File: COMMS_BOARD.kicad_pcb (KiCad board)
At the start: 4 copper layers, 75 x 55 mm, 107 parts, among them IC1 TCAN1044VDDFR, IC2 BMM350, J1 Conn_Coaxial_Small, J2 Conn_01x02, J3 Conn_01x04, J4 Screw_Terminal_01x02, J5 Conn_01x02, J6 Conn_Coaxial_Small, J7 Conn_01x06, J8 Conn_01x04, U1 MAX31855KASA, U2 SA818V, U3 ESP32-WROOM-32E, U4 MAX-M10S, U5 USBLC6-2SC6, U6 MS5611-01BA

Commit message: ADDE IMU
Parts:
- removed D3, D8: PESD3V3Z1BCSFYL, SamacSys_Parts:PMEG3005AESFYL
- added C28: 100nF, Capacitor_SMD:C_0603_1608Metric, F.Cu at (155.2, 78.2)
- added C29: 100nF, Capacitor_SMD:C_0603_1608Metric, F.Cu at (155.3, 80.2)
- added U7: BMI088, Package_LGA:Bosch_LGA-16_4.5x3mm_P0.5mm_LayoutBorder7x1y_ClockwisePinNumbering, F.Cu at (155.1, 83.0)
- J5: value Conn_01x02 -> S2B-PH-SM4-TB_LF__SN_; footprint Connector_JST:JST_XH_B2B-XH-A_1x02_P2.50mm_Vertical -> SamacSys_Parts:S2BPHSM4TBLFSN; moved to B.Cu
- J7: value Conn_01x06 -> Conn_01x04; footprint Connector_JST:JST_PH_B6B-PH-K_1x06_P2.00mm_Vertical -> Connector_JST:JST_PH_S4B-PH-K_1x04_P2.00mm_Horizontal
- R3: moved to F.Cu
- moved R10 8.40 mm to (146.4, 78.8), turned to -90 degrees
- moved R9 8.36 mm to (146.4, 82.0), turned to 90 degrees
- moved J5 6.97 mm to (141.7, 100.2)
- moved C25 5.27 mm to (160.3, 102.8)
- moved C26 5.27 mm to (156.7, 100.1)
- moved C27 5.27 mm to (161.7, 100.0)
- moved IC2 5.27 mm to (159.2, 99.8)
- moved C23 5.10 mm to (158.4, 93.7)
- moved C24 5.10 mm to (156.6, 93.7)
- moved U6 5.10 mm to (161.2, 93.8)
- moved C3 4.50 mm to (165.7, 74.3)
- moved R3 2.95 mm to (144.2, 78.8), turned to 90 degrees
- moved J7 2.87 mm to (142.9, 87.9)
- moved R2 2.11 mm to (167.6, 74.2), turned to 90 degrees
- moved S2 1.26 mm to (140.2, 80.3)
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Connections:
- J5 pad 1: CAN+ -> CAN-
- J5 pad 2: CAN- -> CAN+
- J7 pad 4: CUTTER_EN -> GND
- U3 pad 6: CUTTER_EN -> INT1_ACCEL
- U3 pad 7: VTX_EN -> INT1_GYRO
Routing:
- net VTX_EN: track 45.2 -> 0.00 mm, vias 2 -> 0
- net CUTTER_EN: track 44.1 -> 0.00 mm, vias 2 -> 0
- net I2C_SDL: track 89.4 -> 109.0 mm, vias 11 -> 10
- net INT1_ACCEL: track 0.00 -> 17.0 mm, vias 0 -> 1
- net I2C_SDA: track 84.0 -> 97.0 mm
- net GND: track 69.0 -> 80.2 mm, vias 416 -> 290
- net INT1_GYRO: track 0.00 -> 10.0 mm, vias 0 -> 1
- net BOOT: track 45.4 -> 53.1 mm, vias 1 -> 2
- net +3V3: track 45.7 -> 50.1 mm, vias 35 -> 37
- net CAN-: track 23.9 -> 27.8 mm, vias 0 -> 2
- net CAN+: track 23.8 -> 27.4 mm
- net I2C2_SDL: track 42.2 -> 40.5 mm
- net I2C2_SDA: track 41.1 -> 39.6 mm
- net CAM_SWITCH: track 21.2 -> 22.0 mm
- net UART2_TX: track 39.4 -> 38.6 mm
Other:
- board text added: "CANH"
- board text added: "CANL"
- board text added: "X"
- board text added: "Y"
- board text removed: "CAN"
- board text removed: "CUTTER"
- board text removed: "L"
- board text removed: "PGM"
- board text removed: "VTX_EN"

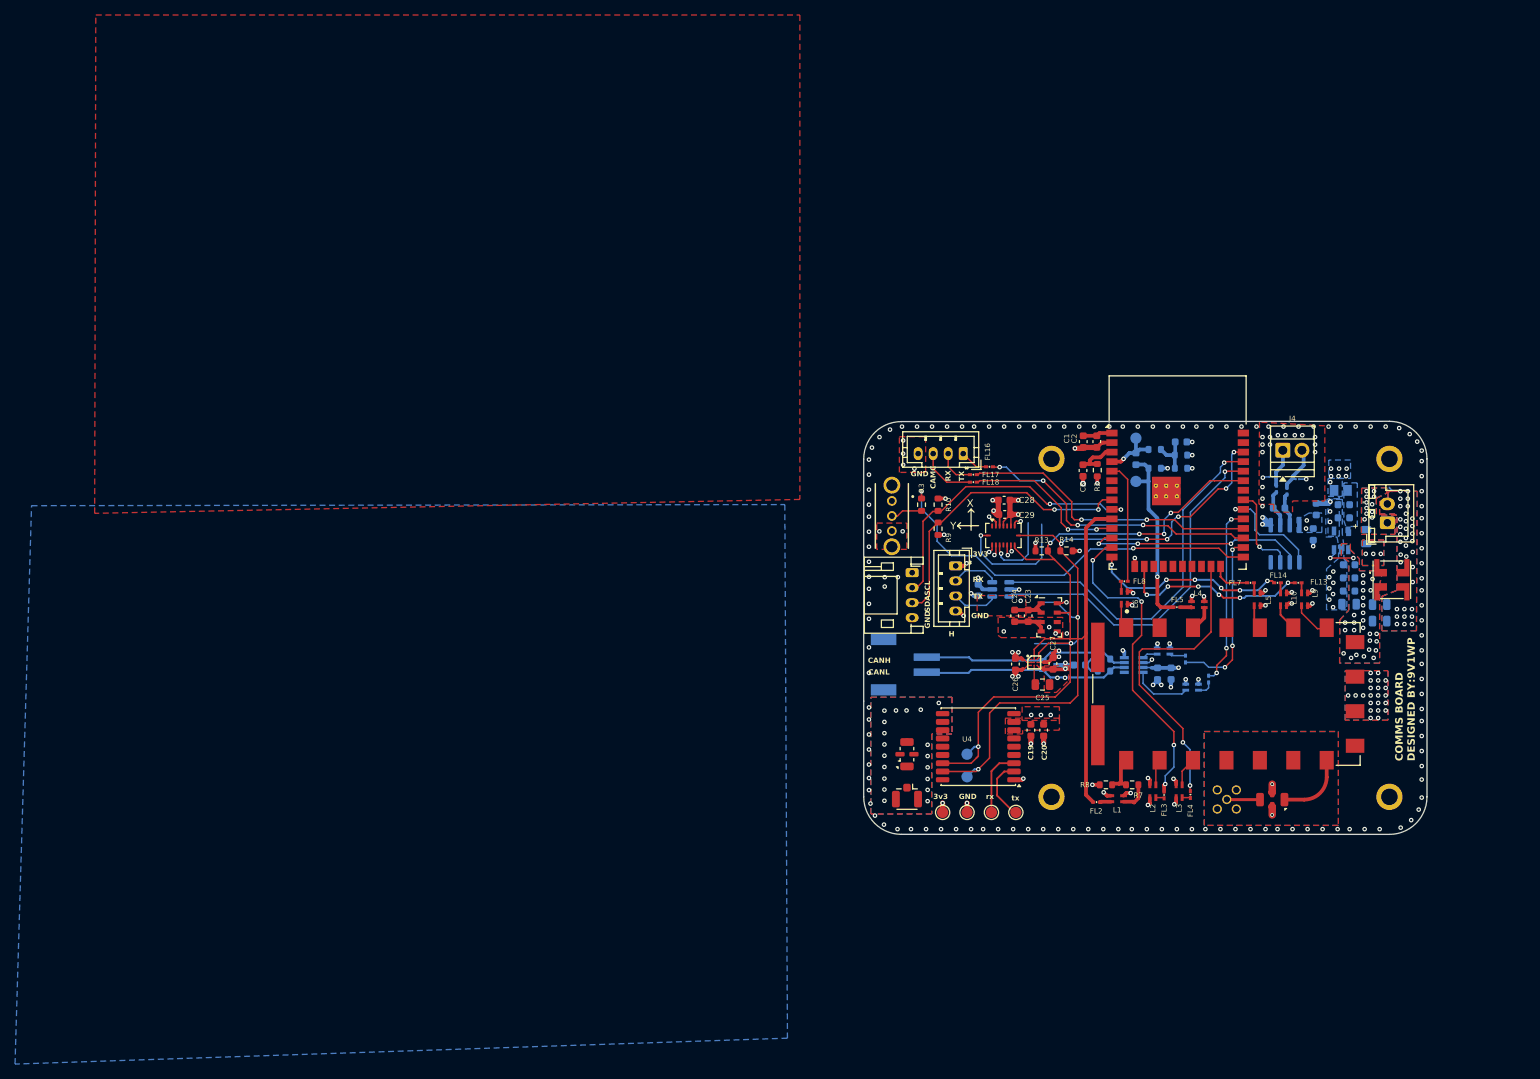
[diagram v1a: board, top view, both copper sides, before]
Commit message: REV2 RELEASE
IO34 AND 35 are inputs, so these are interrupts from IMU
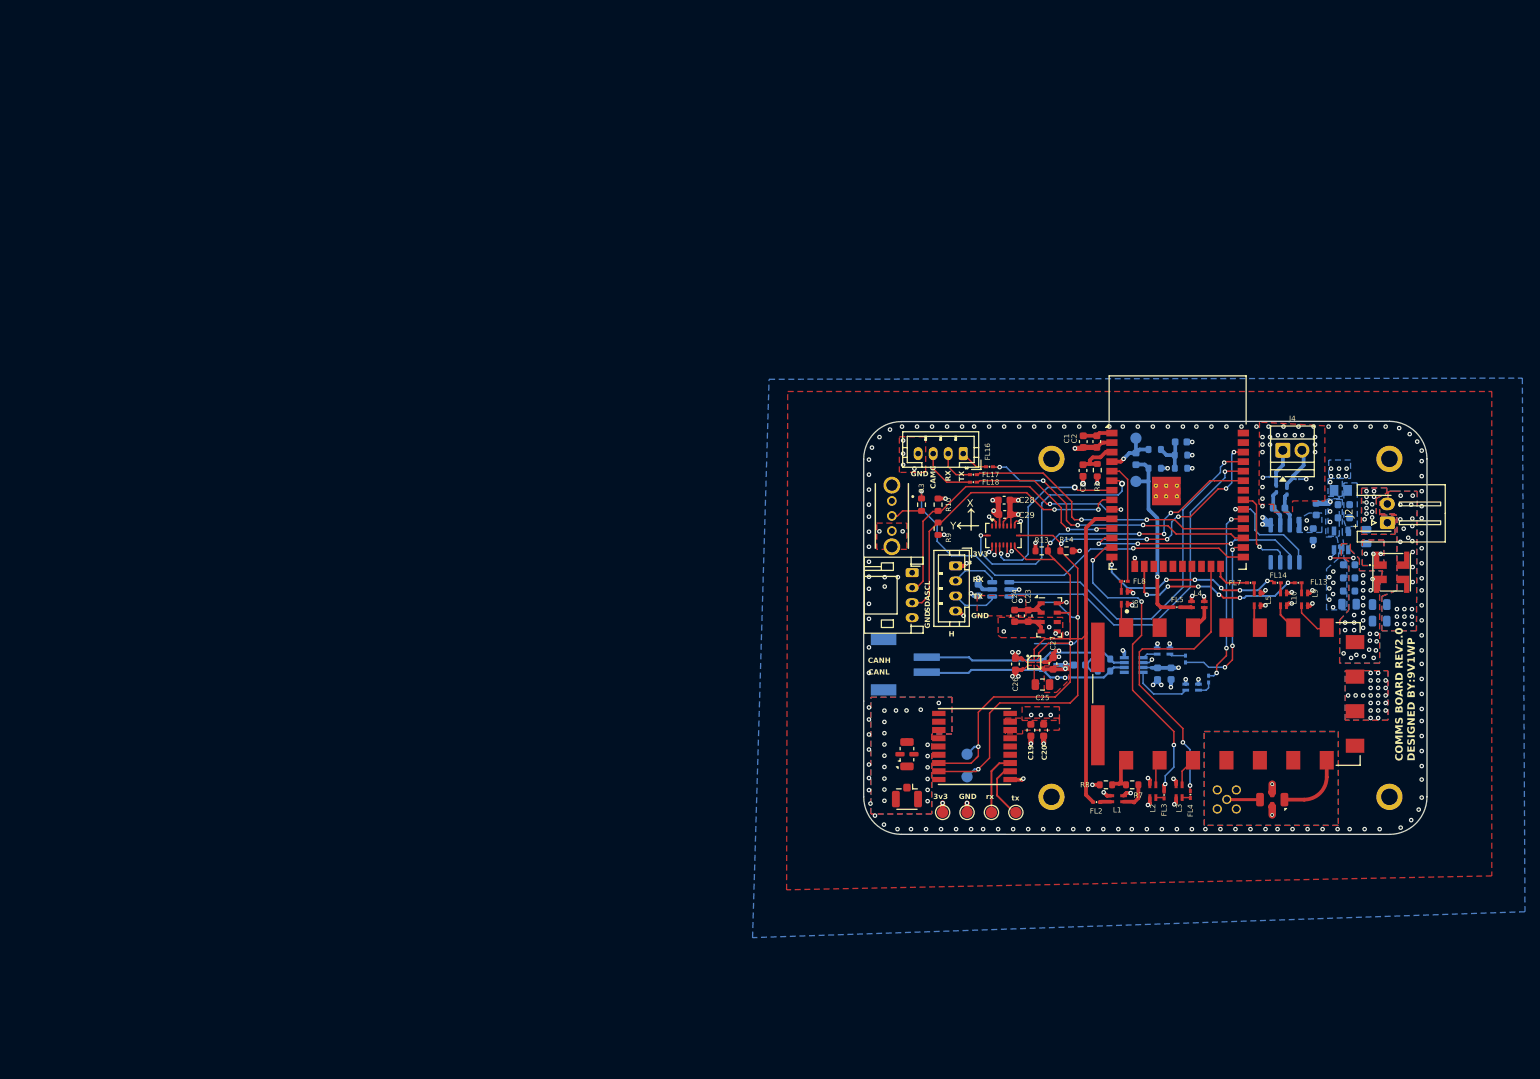
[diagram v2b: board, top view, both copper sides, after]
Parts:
- removed D6: PESD5V0H1BSFYL, SamacSys_Parts:PMEG3005AESFYL
- removed FL6: DLW5ATN112MQ2L, SamacSys_Parts:DLW5BSN302SQ2L
- removed U4: MAX-M10S, RF_GPS:ublox_MAX
- added FL19: DLW5ATH111TQ2L, SamacSys_Parts:DLW5BSN302SQ2L, F.Cu at (206.6, 87.8)
- added IC3: MAX-M10S-00B, SamacSys_Parts:MAXM10S00B, F.Cu at (151.2, 111.0)
- J2: footprint Connector_JST:JST_XH_B2B-XH-A_1x02_P2.50mm_Vertical -> Connector_JST:JST_XH_S2B-XH-A-1_1x02_P2.50mm_Horizontal
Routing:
- net INT1_ACCEL: track 17.0 -> 33.6 mm, vias 1 -> 2
- net INT1_GYRO: track 10.0 -> 24.5 mm, vias 1 -> 2
- net GND: track 80.2 -> 79.6 mm, vias 290 -> 279
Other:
- board text added: "COMMS BOARD REV2.0 DESIGNED BY:9V1WP"
- board text removed: "COMMS BOARD DESIGNED BY:9V1WP"
